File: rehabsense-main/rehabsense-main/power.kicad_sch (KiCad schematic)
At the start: 0 parts

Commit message: update
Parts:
- added J1: B2B-PH-K-S, B2B_PH_K_S:JST_B2B-PH-K-S, symbol B2B-PH-K-S:B2B-PH-K-S
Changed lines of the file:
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@@
 	(generator_version "10.0")
 	(paper "A4")
+	(symbol
+		(lib_id "B2B-PH-K-S:B2B-PH-K-S")
+		(at 138.43 90.17 0)
+		(unit 1)
+		(body_style 1)
+		(exclude_from_sim no)
+		(in_bom yes)
+		(on_board yes)
+		(in_pos_files yes)
+		(dnp no)
+		(fields_autoplaced yes)
+		(property "Reference" "J1"
+			(at 146.05 87.6299 0)
+			(show_name no)
+			(do_not_autoplace no)
+			(effects
+				(font
+					(size 1.27 1.27)
+				)
+				(justify left)
+			)
+		)
+		(property "Value" "B2B-PH-K-S"
+			(at 146.05 90.1699 0)
+			(show_name no)
+			(do_not_autoplace no)
+			(effects
+				(font
+					(size 1.27 1.27)
+				)
+				(justify left)
+			)
+		)
+		(property "Footprint" "B2B_PH_K_S:JST_B2B-PH-K-S"
+			(at 138.43 90.17 0)
+			(hide yes)
+			(show_name no)
+			(do_not_autoplace no)
+			(effects
+				(font
+					(size 1.27 1.27)
+				)
+				(justify bottom)
+			)
+		)
+		(property "Datasheet" ""
+			(at 138.43 90.17 0)
+			(hide yes)
+			(show_name no)
+			(do_not_autoplace no)
+			(effects
+				(font
+					(size 1.27 1.27)
+				)
+			)
+		)
+		(property "Description" ""
+			(at 138.43 90.17 0)
+			(hide yes)
+			(show_name no)
+			(do_not_autoplace no)
+			(effects
+				(font
+					(size 1.27 1.27)
+				)
+			)
+		)
+		(property "MANUFACTURER" "JST"
+			(at 138.43 90.17 0)
+			(hide yes)
+			(show_name no)
+			(do_not_autoplace no)
+			(effects
+				(font
+					(size 1.27 1.27)
+				)
+				(justify bottom)
+			)
+		)
+		(pin "1"
+		)
+		(pin "2"
+		)
+		(instances
+			(project "rehabsense-main"
+				(path "/b751250a-7d43-475a-8447-686d399cd67b/b0bb90cb-8dc9-410c-88d7-96c075ed51f1"
+					(reference "J1")
+					(unit 1)
+				)
+			)
+		)
+	)
 )

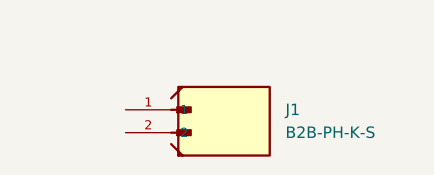
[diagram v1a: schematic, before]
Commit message: Adding adcs
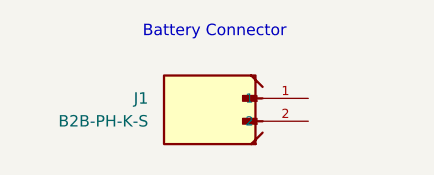
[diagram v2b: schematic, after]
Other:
- note added: "Battery Connector"
- moved on the sheet: J1
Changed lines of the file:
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@@
 	(generator_version "10.0")
 	(paper "A4")
+	(text "Battery Connector"
+		(exclude_from_sim no)
+		(at 138.176 78.994 0)
+		(effects
+			(font
+				(size 1.27 1.27)
+			)
+		)
+	)
 	(symbol
 		(lib_id "B2B-PH-K-S:B2B-PH-K-S")
-		(at 138.43 90.17 0)
+		(at 138.43 88.9 0)
+		(mirror y)
 		(unit 1)
 		(body_style 1)
@@
 		(fields_autoplaced yes)
 		(property "Reference" "J1"
-			(at 146.05 87.6299 0)
+			(at 130.81 86.3599 0)
 			(show_name no)
 			(do_not_autoplace no)
@@
 		)
 		(property "Value" "B2B-PH-K-S"
-			(at 146.05 90.1699 0)
+			(at 130.81 88.8999 0)
 			(show_name no)
 			(do_not_autoplace no)
@@
 		)
 		(property "Footprint" "B2B_PH_K_S:JST_B2B-PH-K-S"
-			(at 138.43 90.17 0)
+			(at 138.43 88.9 0)
 			(hide yes)
 			(show_name no)
@@
 		)
 		(property "Datasheet" ""
-			(at 138.43 90.17 0)
+			(at 138.43 88.9 0)
 			(hide yes)
 			(show_name no)
@@
 		)
 		(property "Description" ""
-			(at 138.43 90.17 0)
+			(at 138.43 88.9 0)
 			(hide yes)
 			(show_name no)
@@
 		)
 		(property "MANUFACTURER" "JST"
-			(at 138.43 90.17 0)
+			(at 138.43 88.9 0)
 			(hide yes)
 			(show_name no)
